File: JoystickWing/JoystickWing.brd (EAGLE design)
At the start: 32.7 x 69.8 mm, 21 parts, among them J1 5747844-4

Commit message: Updated to fix errors and sent to PCBWay
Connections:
- net N$2 renamed PIN6
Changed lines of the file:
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@@
 <layer number="14" name="Route14" color="1" fill="6" visible="no" active="no"/>
 <layer number="15" name="Route15" color="4" fill="6" visible="no" active="no"/>
-<layer number="16" name="Bottom" color="1" fill="1" visible="no" active="yes"/>
+<layer number="16" name="Bottom" color="1" fill="1" visible="yes" active="yes"/>
 <layer number="17" name="Pads" color="2" fill="1" visible="yes" active="yes"/>
 <layer number="18" name="Vias" color="2" fill="1" visible="yes" active="yes"/>
 <layer number="19" name="Unrouted" color="6" fill="1" visible="yes" active="yes"/>
 <layer number="20" name="Dimension" color="24" fill="1" visible="yes" active="yes"/>
-<layer number="21" name="tPlace" color="7" fill="1" visible="yes" active="yes"/>
-<layer number="22" name="bPlace" color="7" fill="1" visible="no" active="yes"/>
-<layer number="23" name="tOrigins" color="15" fill="1" visible="yes" active="yes"/>
-<layer number="24" name="bOrigins" color="15" fill="1" visible="no" active="yes"/>
-<layer number="25" name="tNames" color="7" fill="1" visible="yes" active="yes"/>
-<layer number="26" name="bNames" color="7" fill="1" visible="no" active="yes"/>
+<layer number="21" name="tPlace" color="7" fill="1" visible="no" active="yes"/>
+<layer number="22" name="bPlace" color="7" fill="1" visible="yes" active="yes"/>
+<layer number="23" name="tOrigins" color="15" fill="1" visible="no" active="yes"/>
+<layer number="24" name="bOrigins" color="15" fill="1" visible="yes" active="yes"/>
+<layer number="25" name="tNames" color="7" fill="1" visible="no" active="yes"/>
+<layer number="26" name="bNames" color="7" fill="1" visible="yes" active="yes"/>
 <layer number="27" name="tValues" color="7" fill="1" visible="no" active="yes"/>
 <layer number="28" name="bValues" color="7" fill="1" visible="no" active="yes"/>
@@
 <layer number="37" name="tTest" color="7" fill="1" visible="no" active="yes"/>
 <layer number="38" name="bTest" color="7" fill="1" visible="no" active="yes"/>
-<layer number="39" name="tKeepout" color="4" fill="11" visible="yes" active="yes"/>
-<layer number="40" name="bKeepout" color="1" fill="11" visible="no" active="yes"/>
-<layer number="41" name="tRestrict" color="4" fill="10" visible="yes" active="yes"/>
-<layer number="42" name="bRestrict" color="1" fill="10" visible="no" active="yes"/>
+<layer number="39" name="tKeepout" color="4" fill="11" visible="no" active="yes"/>
+<layer number="40" name="bKeepout" color="1" fill="11" visible="yes" active="yes"/>
+<layer number="41" name="tRestrict" color="4" fill="10" visible="no" active="yes"/>
+<layer number="42" name="bRestrict" color="1" fill="10" visible="yes" active="yes"/>
 <layer number="43" name="vRestrict" color="2" fill="10" visible="no" active="yes"/>
 <layer number="44" name="Drills" color="7" fill="1" visible="no" active="yes"/>
@@
 <layer number="49" name="Reference" color="7" fill="1" visible="no" active="yes"/>
 <layer number="50" name="dxf" color="7" fill="1" visible="no" active="no"/>
-<layer number="51" name="tDocu" color="7" fill="1" visible="yes" active="yes"/>
-<layer number="52" name="bDocu" color="7" fill="1" visible="no" active="yes"/>
+<layer number="51" name="tDocu" color="7" fill="1" visible="no" active="yes"/>
+<layer number="52" name="bDocu" color="7" fill="1" visible="yes" active="yes"/>
 <layer number="53" name="tGND_GNDA" color="7" fill="9" visible="no" active="no"/>
 <layer number="54" name="bGND_GNDA" color="1" fill="9" visible="no" active="no"/>
@@
 <wire x1="2.559" y1="39.37" x2="6.35" y2="39.37" width="0.508" layer="1"/>
 </signal>
-<signal name="N$2">
+<signal name="PIN6">
 <contactref element="MS1" pad="20"/>
 <contactref element="JP1" pad="4"/>

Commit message: Removed Adafruit Logos
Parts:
- removed U$10, U$11: (no value), microbuilder:ADAFRUIT_3.5MM
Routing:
- net SDA: track 50.5 -> 47.9 mm
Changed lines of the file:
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@@
 <layer number="14" name="Route14" color="1" fill="6" visible="no" active="no"/>
 <layer number="15" name="Route15" color="4" fill="6" visible="no" active="no"/>
-<layer number="16" name="Bottom" color="1" fill="1" visible="yes" active="yes"/>
+<layer number="16" name="Bottom" color="1" fill="1" visible="no" active="yes"/>
 <layer number="17" name="Pads" color="2" fill="1" visible="yes" active="yes"/>
 <layer number="18" name="Vias" color="2" fill="1" visible="yes" active="yes"/>
 <layer number="19" name="Unrouted" color="6" fill="1" visible="yes" active="yes"/>
 <layer number="20" name="Dimension" color="24" fill="1" visible="yes" active="yes"/>
-<layer number="21" name="tPlace" color="7" fill="1" visible="no" active="yes"/>
-<layer number="22" name="bPlace" color="7" fill="1" visible="yes" active="yes"/>
-<layer number="23" name="tOrigins" color="15" fill="1" visible="no" active="yes"/>
-<layer number="24" name="bOrigins" color="15" fill="1" visible="yes" active="yes"/>
-<layer number="25" name="tNames" color="7" fill="1" visible="no" active="yes"/>
-<layer number="26" name="bNames" color="7" fill="1" visible="yes" active="yes"/>
+<layer number="21" name="tPlace" color="7" fill="1" visible="yes" active="yes"/>
+<layer number="22" name="bPlace" color="7" fill="1" visible="no" active="yes"/>
+<layer number="23" name="tOrigins" color="15" fill="1" visible="yes" active="yes"/>
+<layer number="24" name="bOrigins" color="15" fill="1" visible="no" active="yes"/>
+<layer number="25" name="tNames" color="7" fill="1" visible="yes" active="yes"/>
+<layer number="26" name="bNames" color="7" fill="1" visible="no" active="yes"/>
 <layer number="27" name="tValues" color="7" fill="1" visible="no" active="yes"/>
 <layer number="28" name="bValues" color="7" fill="1" visible="no" active="yes"/>
@@
 <layer number="37" name="tTest" color="7" fill="1" visible="no" active="yes"/>
 <layer number="38" name="bTest" color="7" fill="1" visible="no" active="yes"/>
-<layer number="39" name="tKeepout" color="4" fill="11" visible="no" active="yes"/>
-<layer number="40" name="bKeepout" color="1" fill="11" visible="yes" active="yes"/>
-<layer number="41" name="tRestrict" color="4" fill="10" visible="no" active="yes"/>
-<layer number="42" name="bRestrict" color="1" fill="10" visible="yes" active="yes"/>
+<layer number="39" name="tKeepout" color="4" fill="11" visible="yes" active="yes"/>
+<layer number="40" name="bKeepout" color="1" fill="11" visible="no" active="yes"/>
+<layer number="41" name="tRestrict" color="4" fill="10" visible="yes" active="yes"/>
+<layer number="42" name="bRestrict" color="1" fill="10" visible="no" active="yes"/>
 <layer number="43" name="vRestrict" color="2" fill="10" visible="no" active="yes"/>
 <layer number="44" name="Drills" color="7" fill="1" visible="no" active="yes"/>
@@
 <layer number="49" name="Reference" color="7" fill="1" visible="no" active="yes"/>
 <layer number="50" name="dxf" color="7" fill="1" visible="no" active="no"/>
-<layer number="51" name="tDocu" color="7" fill="1" visible="no" active="yes"/>
-<layer number="52" name="bDocu" color="7" fill="1" visible="yes" active="yes"/>
+<layer number="51" name="tDocu" color="7" fill="1" visible="yes" active="yes"/>
+<layer number="52" name="bDocu" color="7" fill="1" visible="no" active="yes"/>
 <layer number="53" name="tGND_GNDA" color="7" fill="9" visible="no" active="no"/>
 <layer number="54" name="bGND_GNDA" color="1" fill="9" visible="no" active="no"/>
@@
 <text x="12.7" y="40.03675" size="1.016" layer="21" font="vector" ratio="14" align="center">RL</text>
 <text x="16.51" y="36.576" size="1.4732" layer="21" font="vector" ratio="15" align="center">DS3502</text>
-<text x="19.05" y="35.052" size="1.016" layer="21" font="vector" ratio="15" align="center">I2C Potentiometer</text>
+<text x="16.95" y="35.052" size="1.016" layer="21" font="vector" ratio="15" align="center">I2C Potentiometer</text>
 <wire x1="6.35" y1="39.37" x2="8.509" y2="41.529" width="0.3556" layer="22"/>
 <wire x1="8.509" y1="41.529" x2="8.509" y2="45.085" width="0.3556" layer="22"/>
@@
 <attribute name="VALUE" x="8.89" y="3.048" size="0.4064" layer="27" ratio="10"/>
 </element>
-<element name="U$10" library="microbuilder" package="ADAFRUIT_3.5MM" value="" x="21.479" y="16.641" smashed="yes"/>
 <element name="JP5" library="microbuilder" package="1X04_ROUND" value="" x="16.51" y="38.481" smashed="yes">
 <attribute name="VALUE" x="11.43" y="35.306" size="0.4064" layer="27" ratio="10"/>
@@
 <attribute name="VALUE" x="8.89" y="22.606" size="0.4064" layer="27" ratio="10"/>
 </element>
-<element name="U$11" library="microbuilder" package="ADAFRUIT_3.5MM" value="" x="8.579" y="33.899" smashed="yes"/>
 <element name="JP1" library="adafruit" library_urn="urn:adsk.eagle:library:420" package="1X12" package3d_urn="urn:adsk.eagle:package:6240771/1" value="" x="2.559" y="30.48" smashed="yes" rot="R270">
 <attribute name="NAME" x="4.3878" y="45.7962" size="1.27" layer="25" ratio="10" rot="R270"/>
@@
 <contactref element="JP3" pad="4"/>
 <contactref element="JP5" pad="4"/>
-<wire x1="21.463" y1="26.25445" x2="21.463" y2="25.30755" width="0.3048" layer="1"/>
 <wire x1="20.32" y1="38.481" x2="20.32" y2="27.39745" width="0.3048" layer="1"/>
-<wire x1="20.32" y1="24.16455" x2="20.32" y2="18.923" width="0.3048" layer="1"/>
+<wire x1="21.463" y1="26.25445" x2="21.463" y2="20.066" width="0.3048" layer="1"/>
+<wire x1="20.32" y1="18.923" x2="21.463" y2="20.066" width="0.3048" layer="1"/>
 <wire x1="20.32" y1="27.39745" x2="21.463" y2="26.25445" width="0.3048" layer="1"/>
-<wire x1="21.463" y1="25.30755" x2="20.32" y2="24.16455" width="0.3048" layer="1"/>
 <wire x1="15.1384" y1="61.7728" x2="16.71955" y2="60.19165" width="0.508" layer="16"/>
 <wire x1="16.71955" y1="60.19165" x2="17.033425" y2="60.19165" width="0.508" layer="16"/>
@@
 <via x="9.636609375" y="40.624609375" extent="1-16" drill="0.35"/>
 <wire x1="17.78" y1="32.73521875" x2="17.78" y2="25.781" width="0.3048" layer="1"/>
-<wire x1="11.557" y1="38.00755" x2="12.22655" y2="37.338" width="0.3048" layer="1"/>
 <wire x1="9.636609375" y1="40.624609375" x2="11.557" y2="38.70421875" width="0.3048" layer="1"/>
 <wire x1="13.17721875" y1="37.338" x2="17.78" y2="32.73521875" width="0.3048" layer="1"/>
-<wire x1="11.557" y1="38.70421875" x2="11.557" y2="38.00755" width="0.3048" layer="1"/>
-<wire x1="12.22655" y1="37.338" x2="13.17721875" y2="37.338" width="0.3048" layer="1"/>
 <contactref element="JP1" pad="1"/>
 <wire x1="16.51" y1="17.653" x2="16.51" y2="24.5006" width="0.3048" layer="16"/>
@@
 <wire x1="17.0434" y1="25.0444" x2="17.78" y2="25.781" width="0.3048" layer="16"/>
 <wire x1="2.559" y1="44.45" x2="6.35" y2="44.45" width="0.508" layer="1"/>
+<wire x1="13.17721875" y1="37.338" x2="11.557" y2="38.70421875" width="0" layer="19" extent="1-1"/>
 </signal>
 <signal name="VCC">

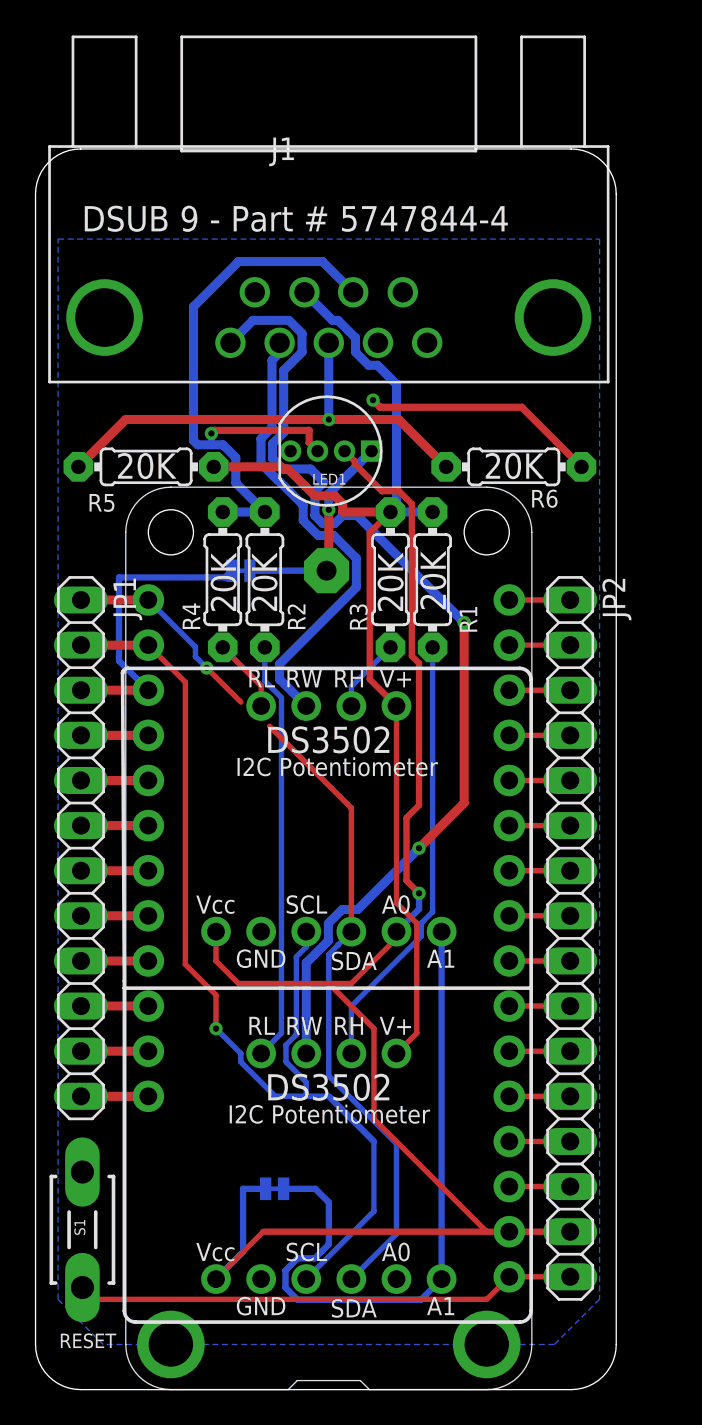
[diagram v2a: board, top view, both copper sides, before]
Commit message: Removed bad V+ connection and cleaned up
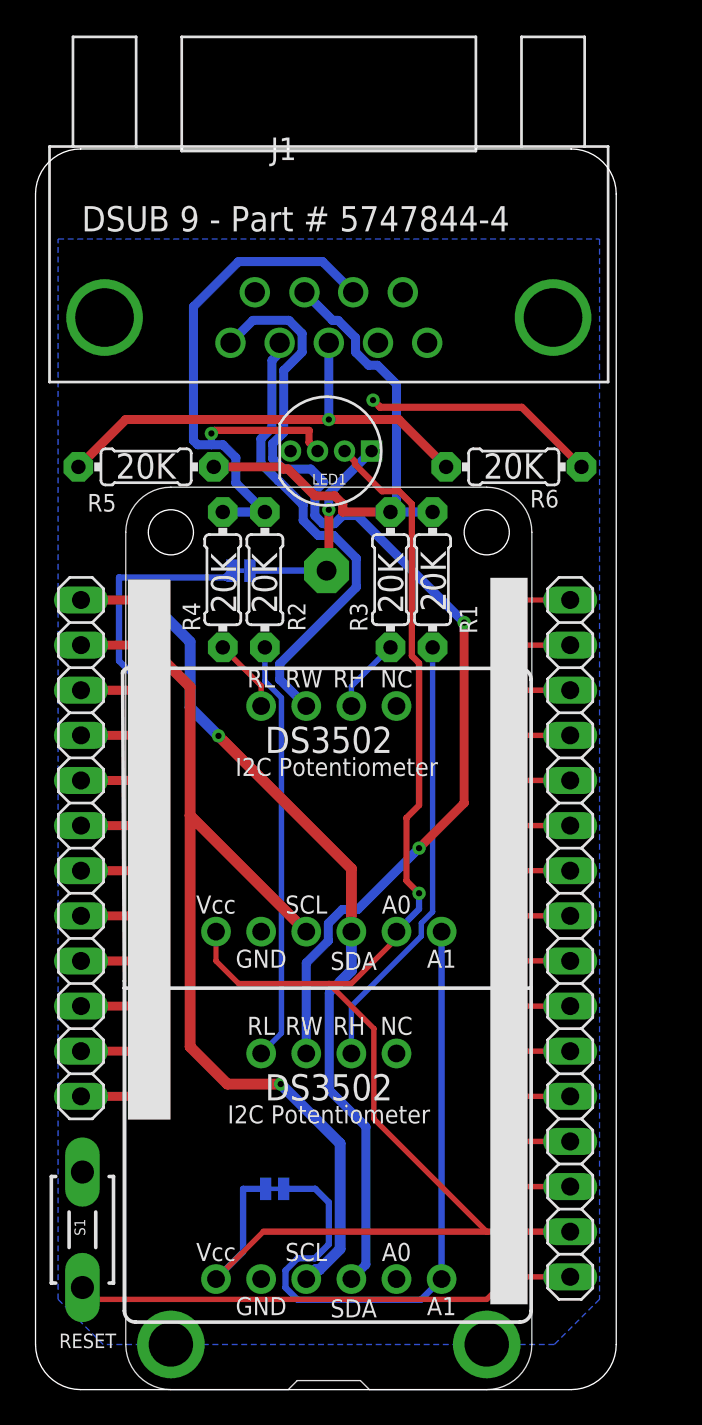
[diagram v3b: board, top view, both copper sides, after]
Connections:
- net +12V: no longer JP3.4, JP5.4
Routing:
- net +12V: track 61.3 -> 28.8 mm
- net SCL: track 58.3 -> 55.9 mm
- net SDA: track 47.9 -> 48.5 mm
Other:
- board text added: "NC"
- board text removed: "V+"
